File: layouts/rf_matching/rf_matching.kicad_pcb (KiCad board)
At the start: 2 copper layers, 6 parts

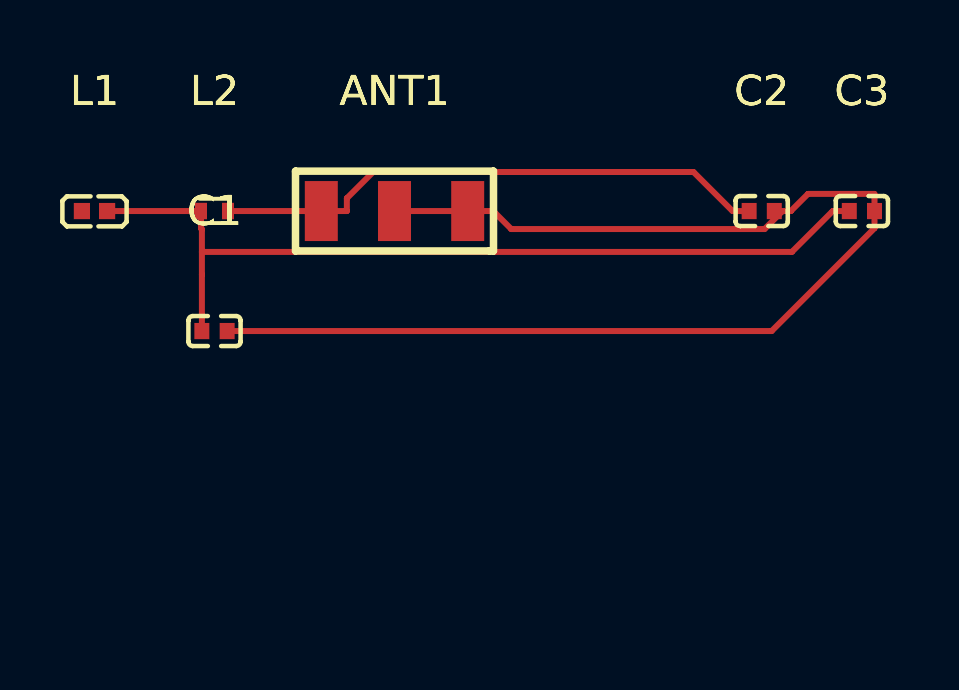
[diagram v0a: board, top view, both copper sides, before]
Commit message: Enhance smart placer with simulated annealing and pre-routing validation
Smart Placer improvements:
- Add simulated annealing refinement (now default) for better wire length optimization
- Add force-directed refinement with improvement safeguard
- Add silkscreen text repositioning to avoid component overlaps
- Significant wire length reductions (e.g., power_filter: 113mm -> 46mm)

Autorouter improvements:
- Add PreRoutingValidator class for pre-flight checks
- Validate unconnected pads, overlapping footprints, unplaced components
- Use pad-based bounds for accurate overlap detection
- Block routing on validation errors with actionable messages

Research:
- Add comprehensive autorouting/autoplacement findings document
- Cover Freerouting Python client, OrthoRoute, DeepPCB, KiCad 9 IPC API
- Document force-directed and simulated annealing algorithms

Cleanup:
- Update .gitignore for DSN/SES files, build artifacts, tools
- Remove stale timestamped build files
- Add parts footprints and symbols

All 10 modules placed and routed successfully.

Co-Authored-By: Claude Opus 4.5 <noreply@anthropic.com>
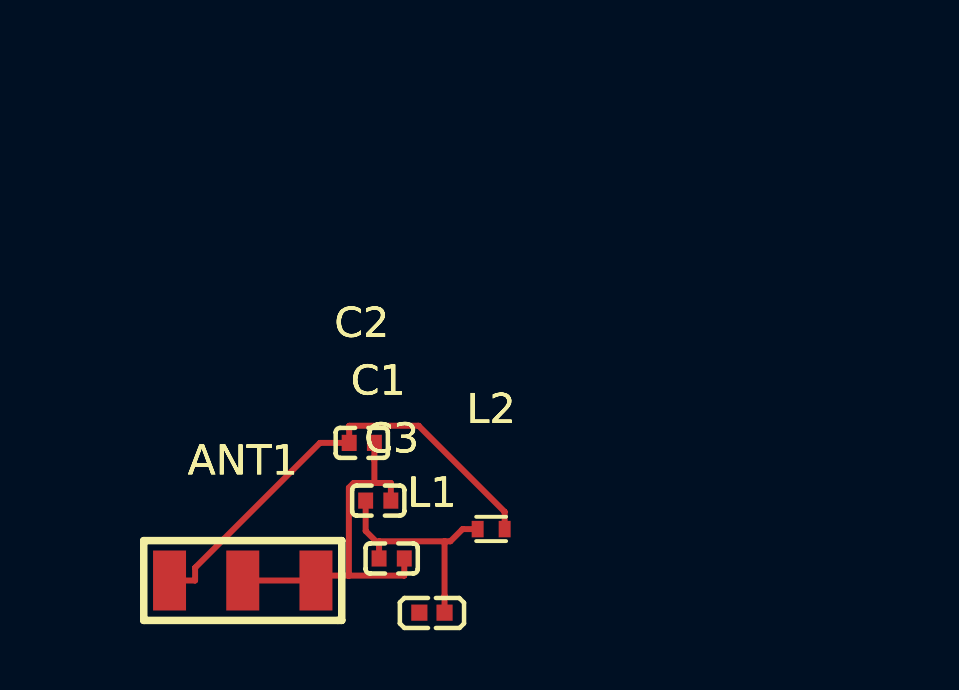
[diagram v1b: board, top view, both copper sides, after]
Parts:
- moved C3 19.5 mm to (99.9, 111.6)
- moved L1 17.5 mm to (101.2, 113.4)
- moved C2 15.4 mm to (98.9, 107.7)
- moved L2 14.1 mm to (103.2, 110.6)
- moved ANT1 13.3 mm to (94.9, 112.3)
- moved C1 7.86 mm to (99.5, 109.7)
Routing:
- net gnd: track 41.2 -> 12.4 mm
- net _1: track 29.3 -> 8.05 mm
- net Feed: track 18.7 -> 15.7 mm
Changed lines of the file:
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@@
 	(footprint "Murata_Electronics_GCM1555C1H3R3GA16D:C0402"
 		(layer "F.Cu")
-		(at 94 104)
+		(at 99.4584 109.6519)
 		(property "Reference" "C1"
 			(at 0 -4 0)
@@
 	(footprint "Murata_Electronics_LQW15AN4N2G80D:IND-SMD_L1.0-W0.5-2"
 		(layer "F.Cu")
-		(at 94 100)
+		(at 103.2213 110.6015)
 		(property "Reference" "L2"
 			(at 0 -4 0)
@@
 	(footprint "Murata_Electronics_GJM1555C1H5R6BB01D:C0402"
 		(layer "F.Cu")
-		(at 115.58 100)
+		(at 99.9056 111.5805)
 		(property "Reference" "C3"
 			(at 0 -4 0)
@@
 	(footprint "Murata_Electronics_GJM1555C1H5R6BB01D:C0402"
 		(layer "F.Cu")
-		(at 112.24 100)
+		(at 98.9095 107.728)
 		(property "Reference" "C2"
 			(at 0 -4 0)
@@
 	(footprint "KYOCERA_AVX_M620720:ANT-SMD_3P-L6.0-W2.0_M620720"
 		(layer "F.Cu")
-		(at 100 100)
+		(at 94.9417 112.3153)
 		(property "Reference" "ANT1"
 			(at 0 -4 0)
@@
 	(footprint "Sunlord_SDCL1005C8N2JTDF:L0402"
 		(layer "F.Cu")
-		(at 90 100)
+		(at 101.2483 113.3871)
 		(property "Reference" "L1"
 			(at 0 -4 0)
@@
 	)
 	(segment
-		(start 109.9666 98.6983)
-		(end 111.2683 100)
+		(start 93.3534 112.3153)
+		(end 93.3534 111.8894)
 		(width 0.2)
 		(layer "F.Cu")
@@
 	)
 	(segment
-		(start 97.56 100)
-		(end 98.4117 100)
+		(start 100.8028 107.1563)
+		(end 98.4895 107.1563)
 		(width 0.2)
 		(layer "F.Cu")
@@
 	)
 	(segment
-		(start 97.56 100)
-		(end 94.45 100)
+		(start 98.4895 107.728)
+		(end 98.4895 107.1563)
 		(width 0.2)
 		(layer "F.Cu")
@@
 	)
 	(segment
-		(start 111.82 100)
-		(end 111.2683 100)
+		(start 92.5017 112.3153)
+		(end 93.3534 112.3153)
 		(width 0.2)
 		(layer "F.Cu")
@@
 	)
 	(segment
-		(start 98.4117 100)
-		(end 98.4117 99.5741)
+		(start 93.3534 111.8894)
+		(end 97.5148 107.728)
 		(width 0.2)
 		(layer "F.Cu")
@@
 	)
 	(segment
-		(start 99.2875 98.6983)
-		(end 109.9666 98.6983)
+		(start 103.6713 110.0248)
+		(end 100.8028 107.1563)
 		(width 0.2)
 		(layer "F.Cu")
@@
 	)
 	(segment
-		(start 98.4117 99.5741)
-		(end 99.2875 98.6983)
+		(start 103.6713 110.6015)
+		(end 103.6713 110.0248)
 		(width 0.2)
 		(layer "F.Cu")
@@
 	)
 	(segment
-		(start 93.58 100.6067)
-		(end 93.55 100.5767)
+		(start 97.5148 107.728)
+		(end 98.4895 107.728)
+		(width 0.2)
+		(layer "F.Cu")
+		(net 1)
+	)
+	(segment
+		(start 101.6683 113.3871)
+		(end 101.6683 112.8154)
 		(width 0.2)
 		(layer "F.Cu")
@@
 	)
 	(segment
-		(start 114.6083 100)
-		(end 113.2458 101.3625)
+		(start 99.4856 111.0088)
+		(end 101.6683 111.0088)
 		(width 0.2)
 		(layer "F.Cu")
@@
 	)
 	(segment
-		(start 93.55 100)
-		(end 93.55 100.5767)
+		(start 99.4856 111.5805)
+		(end 99.4856 111.112)
 		(width 0.2)
 		(layer "F.Cu")
@@
 	)
 	(segment
-		(start 93.58 102.1183)
-		(end 93.58 101.3625)
+		(start 99.0384 110.6648)
+		(end 99.0384 109.6519)
 		(width 0.2)
 		(layer "F.Cu")
@@
 	)
 	(segment
-		(start 93.58 104)
-		(end 93.58 102.1183)
+		(start 101.8623 111.0088)
+		(end 102.2696 110.6015)
 		(width 0.2)
 		(layer "F.Cu")
@@
 	)
 	(segment
-		(start 93.58 101.3625)
-		(end 93.58 100.6067)
+		(start 99.4856 111.112)
+		(end 99.0384 110.6648)
 		(width 0.2)
 		(layer "F.Cu")
@@
 	)
 	(segment
-		(start 115.16 100)
-		(end 114.6083 100)
+		(start 102.7713 110.6015)
+		(end 102.2696 110.6015)
 		(width 0.2)
 		(layer "F.Cu")
@@
 	)
 	(segment
-		(start 93.55 100)
-		(end 90.42 100)
+		(start 99.4856 111.112)
+		(end 99.4856 111.0088)
 		(width 0.2)
 		(layer "F.Cu")
@@
 	)
 	(segment
-		(start 113.2458 101.3625)
-		(end 93.58 101.3625)
+		(start 101.6683 111.0088)
+		(end 101.8623 111.0088)
 		(width 0.2)
 		(layer "F.Cu")
@@
 	)
 	(segment
-		(start 112.336 100.5999)
-		(end 103.8916 100.5999)
+		(start 101.6683 112.8154)
+		(end 101.6683 111.0088)
+		(width 0.2)
+		(layer "F.Cu")
+		(net 2)
+	)
+	(segment
+		(start 99.3295 109.0652)
+		(end 99.3295 108.2997)
 		(width 0.2)
 		(layer "F.Cu")
@@
 	)
 	(segment
-		(start 100 100)
-		(end 102.44 100)
+		(start 99.3295 109.0652)
+		(end 98.6358 109.0652)
 		(width 0.2)
 		(layer "F.Cu")
@@
 	)
 	(segment
-		(start 102.44 100)
-		(end 103.2917 100)
+		(start 98.6358 109.0652)
+		(end 98.479 109.222)
 		(width 0.2)
 		(layer "F.Cu")
@@
 	)
 	(segment
-		(start 116 100)
-		(end 116 100.5717)
+		(start 97.3817 112.1522)
+		(end 97.3817 112.3153)
 		(width 0.2)
 		(layer "F.Cu")
@@
 	)
 	(segment
-		(start 116 100.5717)
-		(end 112.5717 104)
+		(start 99.8784 109.0652)
+		(end 99.3295 109.0652)
 		(width 0.2)
 		(layer "F.Cu")
@@
 	)
 	(segment
-		(start 112.9359 100)
-		(end 113.2117 100)
+		(start 100.3256 111.5805)
+		(end 100.3256 112.1522)
 		(width 0.2)
 		(layer "F.Cu")
@@
 	)
 	(segment
-		(start 112.9359 100)
-		(end 112.336 100.5999)
+		(start 99.3295 107.728)
+		(end 99.3295 108.2997)
 		(width 0.2)
 		(layer "F.Cu")
@@
 	)
 	(segment
-		(start 112.66 100)
-		(end 112.9359 100)
+		(start 99.8784 109.6519)
+		(end 99.8784 109.0652)
 		(width 0.2)
 		(layer "F.Cu")
@@
 	)
 	(segment
-		(start 113.7834 99.4283)
-		(end 116 99.4283)
+		(start 98.479 109.222)
+		(end 98.479 112.1522)
 		(width 0.2)
 		(layer "F.Cu")
@@
 	)
 	(segment
-		(start 112.5717 104)
-		(end 94.42 104)
+		(start 98.479 112.1522)
+		(end 100.3256 112.1522)
 		(width 0.2)
 		(layer "F.Cu")
@@
 	)
 	(segment
-		(start 103.8916 100.5999)
-		(end 103.2917 100)
+		(start 97.3817 112.1522)
+		(end 98.479 112.1522)
 		(width 0.2)
 		(layer "F.Cu")
@@
 	)
 	(segment
-		(start 116 100)
-		(end 116 99.4283)
-		(width 0.2)
-		(layer "F.Cu")
-		(net 3)
-	)
-	(segment
-		(start 113.2117 100)
-		(end 113.7834 99.4283)
-		(width 0.2)
-		(layer "F.Cu")
+		(start 94.9417 112.3153)
+		(end 97.3817 112.3153)
+		(width 0.2)
+		(layer "F.Cu")
